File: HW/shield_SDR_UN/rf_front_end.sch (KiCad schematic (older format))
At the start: 73 parts, among them P1 GSG-RF-CONN, P2 GSG-RF-CONN, Q1 MOSFET_P, T1 BALUN, T2 BALUN, U1 MAX2830, U2 SI5351C, U3 MAX5864, X1 GSG-XTAL4PIN

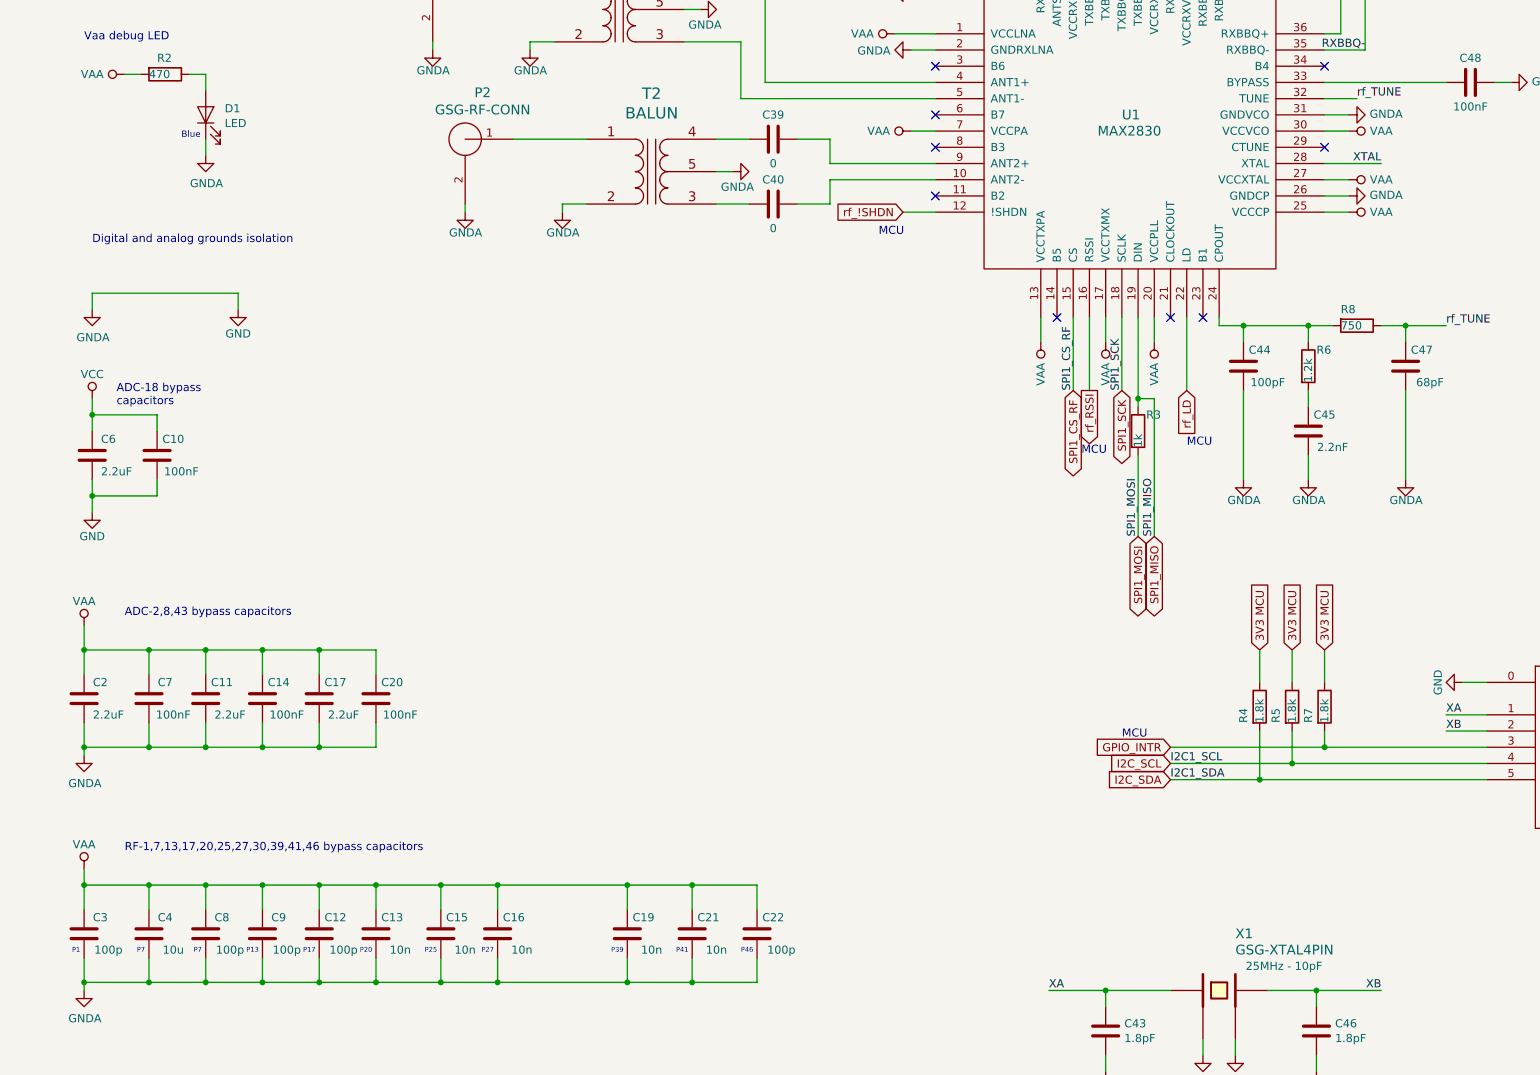
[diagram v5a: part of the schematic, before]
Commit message: Partnumbers modified
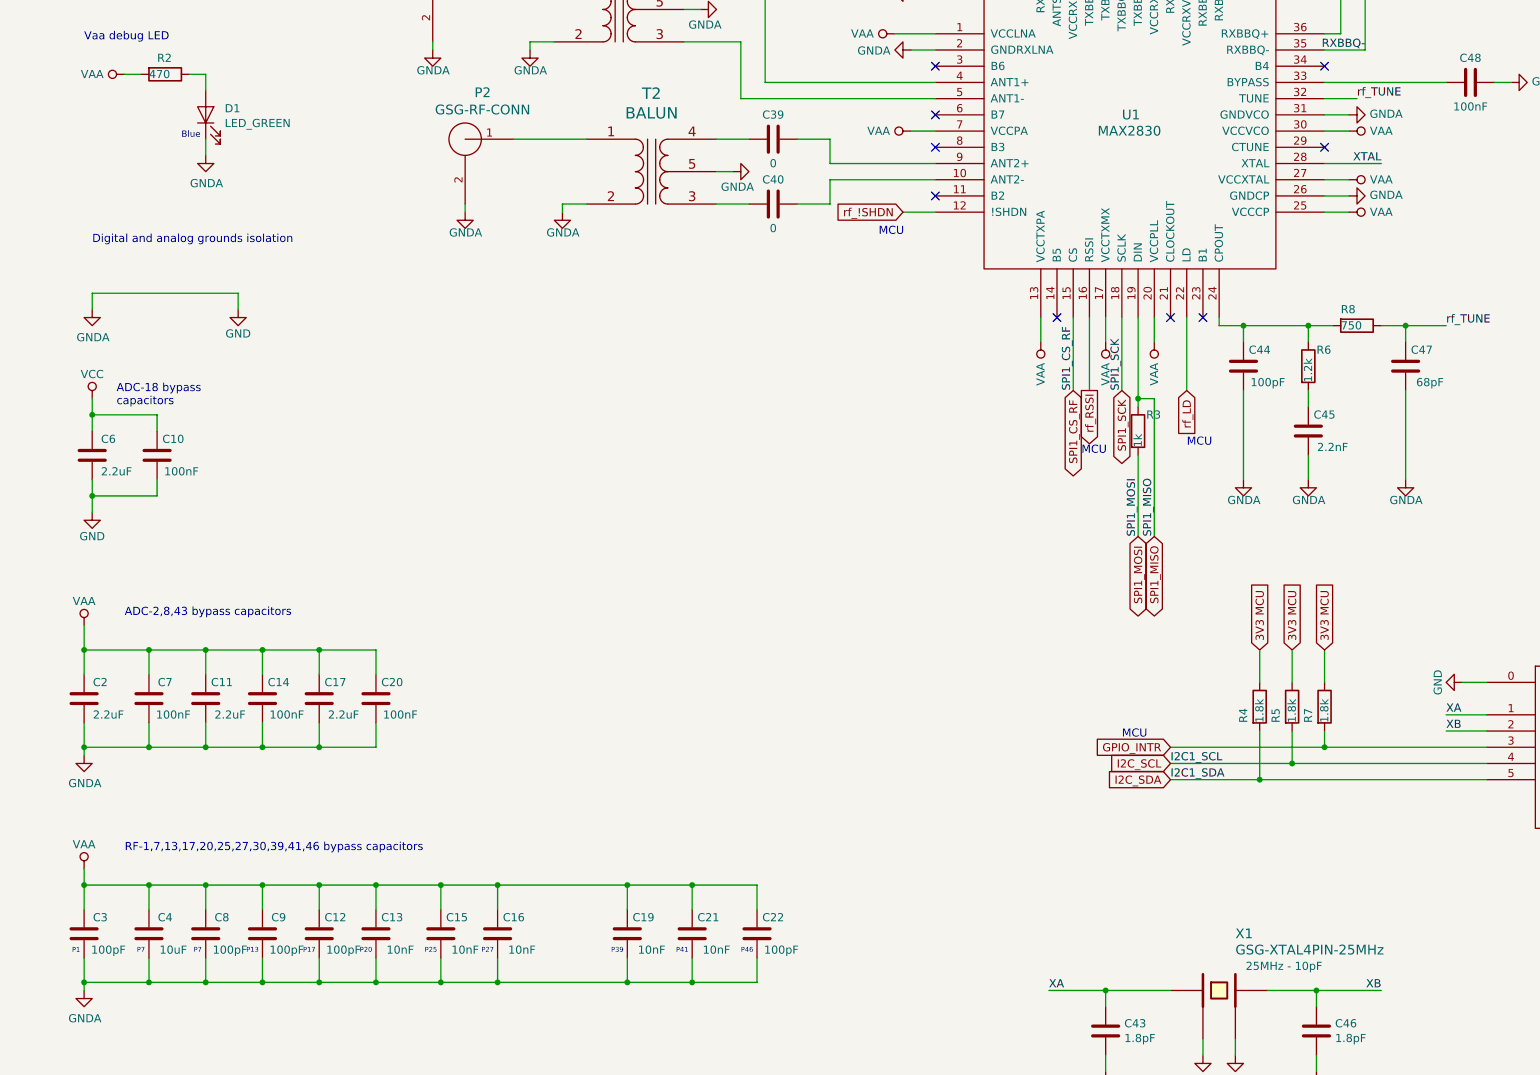
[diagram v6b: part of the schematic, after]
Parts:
- C11, C17, C2, C6: Digikey 1276-1183-1-ND -> 1276-1085-1-ND
- C12, C22, C3, C8, C9: value 100p -> 100pF
- C13, C15, C16, C19, C21: value 10n -> 10nF
- C4: value 10u -> 10uF
- C44: Digikey (none) -> 1276-1909-1-ND
- C47: Digikey (none) -> 1276-6538-1-ND
- C5: Digikey 1276-6456-1-ND -> 1276-1192-1-ND
- D1: value LED -> LED_GREEN; Digikey 160-2032-1-ND -> 160-1468-1-ND
- R21: Digikey (none) -> 311-39.0HRCT-ND
- R3: Digikey (none) -> 311-1.00KHRCT-ND
- R6: Digikey (none) -> 311-1.20KHRCT-ND
- R8: Digikey (none) -> 311-750HRCT-ND
- X1: value GSG-XTAL4PIN -> GSG-XTAL4PIN-25MHz
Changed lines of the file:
@@
 F 2 "Capacitor_SMD:C_0603_1608Metric_Pad1.05x0.95mm_HandSolder" H 1288 2800 50  0001 C CNN
 F 3 "http://www.samsungsem.com/kr/support/product-search/mlcc/__icsFiles/afieldfile/2019/05/10/19-CL10A225KQ8NNNC.pdf" H 1250 2950 50  0001 C CNN
-F 4 "1276-6456-1-ND" H 1250 2950 50  0001 C CNN "Digikey"
+F 4 "1276-1192-1-ND" H 1250 2950 50  0001 C CNN "Digikey"
 	1    1250 2950
 	1    0    0    -1
@@
 F 2 "Capacitor_SMD:C_0603_1608Metric_Pad1.05x0.95mm_HandSolder" H 1288 6200 50  0001 C CNN
 F 3 "http://www.samsungsem.com/kr/support/product-search/mlcc/__icsFiles/afieldfile/2019/05/10/19-CL10A225KQ8NNNC.pdf" H 1250 6350 50  0001 C CNN
-F 4 "1276-1183-1-ND" H 1250 6350 50  0001 C CNN "Digikey"
+F 4 "1276-1085-1-ND" H 1250 6350 50  0001 C CNN "Digikey"
 	1    1250 6350
 	1    0    0    -1
@@
 F 2 "Capacitor_SMD:C_0603_1608Metric_Pad1.05x0.95mm_HandSolder" H 1238 7700 50  0001 C CNN
 F 3 "http://www.samsungsem.com/kr/support/product-search/mlcc/__icsFiles/afieldfile/2019/05/10/19-CL10A225KQ8NNNC.pdf" H 1200 7850 50  0001 C CNN
-F 4 "1276-1183-1-ND" H 1200 7850 50  0001 C CNN "Digikey"
+F 4 "1276-1085-1-ND" H 1200 7850 50  0001 C CNN "Digikey"
 	1    1200 7850
 	1    0    0    -1
@@
 F 2 "Capacitor_SMD:C_0603_1608Metric_Pad1.05x0.95mm_HandSolder" H 1988 7700 50  0001 C CNN
 F 3 "http://www.samsungsem.com/kr/support/product-search/mlcc/__icsFiles/afieldfile/2019/05/10/19-CL10A225KQ8NNNC.pdf" H 1950 7850 50  0001 C CNN
-F 4 "1276-1183-1-ND" H 1950 7850 50  0001 C CNN "Digikey"
+F 4 "1276-1085-1-ND" H 1950 7850 50  0001 C CNN "Digikey"
 	1    1950 7850
 	1    0    0    -1
@@
 F 2 "Capacitor_SMD:C_0603_1608Metric_Pad1.05x0.95mm_HandSolder" H 2688 7700 50  0001 C CNN
 F 3 "http://www.samsungsem.com/kr/support/product-search/mlcc/__icsFiles/afieldfile/2019/05/10/19-CL10A225KQ8NNNC.pdf" H 2650 7850 50  0001 C CNN
-F 4 "1276-1183-1-ND" H 2650 7850 50  0001 C CNN "Digikey"
+F 4 "1276-1085-1-ND" H 2650 7850 50  0001 C CNN "Digikey"
 	1    2650 7850
 	1    0    0    -1
@@
 P 1200 9300
 F 0 "C3" H 1300 9400 50  0000 C CNN
-F 1 "100p" H 1350 9200 50  0000 C CNN
+F 1 "100pF" H 1350 9200 50  0000 C CNN
 F 2 "Capacitor_SMD:C_0603_1608Metric_Pad1.05x0.95mm_HandSolder" H 1238 9150 50  0001 C CNN
 F 3 "http://www.samsungsem.com/kr/support/product-search/mlcc/__icsFiles/afieldfile/2019/05/10/19-CL10A225KQ8NNNC.pdf" H 1200 9300 50  0001 C CNN
@@
 AR Path="/5CC081D2/5CEDF6C9" Ref="D1"  Part="1"
 F 0 "D1" V 1989 4133 50  0000 R CNN
-F 1 "LED" V 1898 4133 50  0000 R CNN
+F 1 "LED_GREEN" V 1898 4133 50  0000 R CNN
 F 2 "LED_SMD:LED_0805_2012Metric_Pad1.15x1.40mm_HandSolder" H 1950 4250 50  0001 C CNN
-F 3 "http://optoelectronics.liteon.com/upload/download/DS22-2000-239/LTST-S220TBKT.pdf" H 1950 4250 50  0001 C CNN
-F 4 "160-2032-1-ND" V 1950 4250 50  0001 C CNN "Digikey"
+F 3 "http://optoelectronics.liteon.com/upload/download/DS22-2000-075/LTST-S220KGKT.pdf" H 1950 4250 50  0001 C CNN
+F 4 "160-1468-1-ND" V 1950 4250 50  0001 C CNN "Digikey"
 	1    1950 4250
 	0    -1   -1   0
@@
 AR Path="/5CC081D2/5CE83378" Ref="X1"  Part="1"
 F 0 "X1" H 8300 10000 60  0000 L CNN
-F 1 "GSG-XTAL4PIN" H 8300 9900 60  0000 L CNN
+F 1 "GSG-XTAL4PIN-25MHz" H 8300 9900 60  0000 L CNN
 F 2 "CRISTAL_4:GSG-XTAL3.2x2.5mm" H 8400 9290 60  0001 C CNN
 F 3 "" H 8200 9650 60  0000 C CNN
@@
 F 2 "Capacitor_SMD:C_0603_1608Metric_Pad1.05x0.95mm_HandSolder" H 8388 5650 50  0001 C CNN
 F 3 "" H 8350 5800 50  0001 C CNN
-F 4 "" H 8350 5800 50  0001 C CNN "Digikey"
+F 4 "1276-1909-1-ND" H 8350 5800 50  0001 C CNN "Digikey"
 	1    8350 5800
 	-1   0    0    1
@@
 F 2 "Resistor_SMD:R_0603_1608Metric_Pad1.05x0.95mm_HandSolder" V 8680 5800 50  0001 C CNN
 F 3 "" H 8750 5800 50  0001 C CNN
-F 4 "" V 8750 5800 50  0001 C CNN "Digikey"
+F 4 "311-1.20KHRCT-ND" H 8750 5800 50  0001 C CNN "Digikey"
 	1    8750 5800
 	1    0    0    -1
@@
 F 2 "Resistor_SMD:R_0603_1608Metric_Pad1.05x0.95mm_HandSolder" V 8980 5550 50  0001 C CNN
 F 3 "" H 9050 5550 50  0001 C CNN
-F 4 "" V 9050 5550 50  0001 C CNN "Digikey"
+F 4 "311-750HRCT-ND" H 9050 5550 50  0001 C CNN "Digikey"
 	1    9050 5550
 	0    1    1    0
@@
 F 2 "Capacitor_SMD:C_0603_1608Metric_Pad1.05x0.95mm_HandSolder" H 9388 5650 50  0001 C CNN
 F 3 "" H 9350 5800 50  0001 C CNN
-F 4 "" H 9350 5800 50  0001 C CNN "Digikey"
+F 4 "1276-6538-1-ND" H 9350 5800 50  0001 C CNN "Digikey"
 	1    9350 5800
 	-1   0    0    1
@@
 F 5 "RC0603FR-0739RL" V 11400 9100 50  0001 C CNN "part numer"
 F 6 "RES SMD 39 OHM 1% 1/10W 0603" V 11400 9100 50  0001 C CNN "descripcion"
+F 7 "311-39.0HRCT-ND" H 11400 9100 50  0001 C CNN "Digikey"
 	1    11400 9100
 	0    1    1    0
@@
 F 2 "Resistor_SMD:R_0603_1608Metric_Pad1.05x0.95mm_HandSolder" V 7630 6200 50  0001 C CNN
 F 3 "" H 7700 6200 50  0001 C CNN
-F 4 "" V 7700 6200 50  0001 C CNN "Digikey"
+F 4 " 311-1.00KHRCT-ND" H 7700 6200 50  0001 C CNN "Digikey"
 	1    7700 6200
 	1    0    0    -1
@@
 P 1600 9300
 F 0 "C4" H 1700 9400 50  0000 C CNN
-F 1 "10u" H 1750 9200 50  0000 C CNN
+F 1 "10uF" H 1750 9200 50  0000 C CNN
 F 2 "Capacitor_SMD:C_0603_1608Metric_Pad1.05x0.95mm_HandSolder" H 1638 9150 50  0001 C CNN
 F 3 "http://www.samsungsem.com/kr/support/product-search/mlcc/__icsFiles/afieldfile/2019/05/10/19-CL10A225KQ8NNNC.pdf" H 1600 9300 50  0001 C CNN
@@
 P 1950 9300
 F 0 "C8" H 2050 9400 50  0000 C CNN
-F 1 "100p" H 2100 9200 50  0000 C CNN
+F 1 "100pF" H 2100 9200 50  0000 C CNN
 F 2 "Capacitor_SMD:C_0603_1608Metric_Pad1.05x0.95mm_HandSolder" H 1988 9150 50  0001 C CNN
 F 3 "http://www.samsungsem.com/kr/support/product-search/mlcc/__icsFiles/afieldfile/2019/05/10/19-CL10A225KQ8NNNC.pdf" H 1950 9300 50  0001 C CNN
@@
 P 2300 9300
 F 0 "C9" H 2400 9400 50  0000 C CNN
-F 1 "100p" H 2450 9200 50  0000 C CNN
+F 1 "100pF" H 2450 9200 50  0000 C CNN
 F 2 "Capacitor_SMD:C_0603_1608Metric_Pad1.05x0.95mm_HandSolder" H 2338 9150 50  0001 C CNN
 F 3 "http://www.samsungsem.com/kr/support/product-search/mlcc/__icsFiles/afieldfile/2019/05/10/19-CL10A225KQ8NNNC.pdf" H 2300 9300 50  0001 C CNN
@@
 P 2650 9300
 F 0 "C12" H 2750 9400 50  0000 C CNN
-F 1 "100p" H 2800 9200 50  0000 C CNN
+F 1 "100pF" H 2800 9200 50  0000 C CNN
 F 2 "Capacitor_SMD:C_0603_1608Metric_Pad1.05x0.95mm_HandSolder" H 2688 9150 50  0001 C CNN
 F 3 "http://www.samsungsem.com/kr/support/product-search/mlcc/__icsFiles/afieldfile/2019/05/10/19-CL10A225KQ8NNNC.pdf" H 2650 9300 50  0001 C CNN
@@
 P 3000 9300
 F 0 "C13" H 3100 9400 50  0000 C CNN
-F 1 "10n" H 3150 9200 50  0000 C CNN
+F 1 "10nF" H 3150 9200 50  0000 C CNN
 F 2 "Capacitor_SMD:C_0603_1608Metric_Pad1.05x0.95mm_HandSolder" H 3038 9150 50  0001 C CNN
 F 3 "http://www.samsungsem.com/kr/support/product-search/mlcc/__icsFiles/afieldfile/2019/05/10/19-CL10A225KQ8NNNC.pdf" H 3000 9300 50  0001 C CNN
@@
 P 3400 9300
 F 0 "C15" H 3500 9400 50  0000 C CNN
-F 1 "10n" H 3550 9200 50  0000 C CNN
+F 1 "10nF" H 3550 9200 50  0000 C CNN
 F 2 "Capacitor_SMD:C_0603_1608Metric_Pad1.05x0.95mm_HandSolder" H 3438 9150 50  0001 C CNN
 F 3 "http://www.samsungsem.com/kr/support/product-search/mlcc/__icsFiles/afieldfile/2019/05/10/19-CL10A225KQ8NNNC.pdf" H 3400 9300 50  0001 C CNN
@@
 P 3750 9300
 F 0 "C16" H 3850 9400 50  0000 C CNN
-F 1 "10n" H 3900 9200 50  0000 C CNN
+F 1 "10nF" H 3900 9200 50  0000 C CNN
 F 2 "Capacitor_SMD:C_0603_1608Metric_Pad1.05x0.95mm_HandSolder" H 3788 9150 50  0001 C CNN
 F 3 "http://www.samsungsem.com/kr/support/product-search/mlcc/__icsFiles/afieldfile/2019/05/10/19-CL10A225KQ8NNNC.pdf" H 3750 9300 50  0001 C CNN
@@
 P 4550 9300
 F 0 "C19" H 4650 9400 50  0000 C CNN
-F 1 "10n" H 4700 9200 50  0000 C CNN
+F 1 "10nF" H 4700 9200 50  0000 C CNN
 F 2 "Capacitor_SMD:C_0603_1608Metric_Pad1.05x0.95mm_HandSolder" H 4588 9150 50  0001 C CNN
 F 3 "http://www.samsungsem.com/kr/support/product-search/mlcc/__icsFiles/afieldfile/2019/05/10/19-CL10A225KQ8NNNC.pdf" H 4550 9300 50  0001 C CNN
@@
 P 4950 9300
 F 0 "C21" H 5050 9400 50  0000 C CNN
-F 1 "10n" H 5100 9200 50  0000 C CNN
+F 1 "10nF" H 5100 9200 50  0000 C CNN
 F 2 "Capacitor_SMD:C_0603_1608Metric_Pad1.05x0.95mm_HandSolder" H 4988 9150 50  0001 C CNN
 F 3 "http://www.samsungsem.com/kr/support/product-search/mlcc/__icsFiles/afieldfile/2019/05/10/19-CL10A225KQ8NNNC.pdf" H 4950 9300 50  0001 C CNN
@@
 P 5350 9300
 F 0 "C22" H 5450 9400 50  0000 C CNN
-F 1 "100p" H 5500 9200 50  0000 C CNN
+F 1 "100pF" H 5500 9200 50  0000 C CNN
 F 2 "Capacitor_SMD:C_0603_1608Metric_Pad1.05x0.95mm_HandSolder" H 5388 9150 50  0001 C CNN
 F 3 "http://www.samsungsem.com/kr/support/product-search/mlcc/__icsFiles/afieldfile/2019/05/10/19-CL10A225KQ8NNNC.pdf" H 5350 9300 50  0001 C CNN
